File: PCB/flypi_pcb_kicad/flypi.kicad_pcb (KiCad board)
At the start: 2 copper layers, 76.1 x 85.1 mm, 44 parts, among them CON1 BARREL_JACK, J12 USB_A, P1 Pelt S1S2, P10 RGB BG-R, P3 Fan-+, P4 Therm -s+, P5 HP1 gnd vcc, P6 HP2 gnd vcc, P7 servo -s+, P8 Ring s-+, P9 I2C +-scsd, Q1 1A_NPN_ECB, Q2 1A-NPN-ECB, Q3 1A_NPN_ECB, Q4 1A_NPN_ECB, U1 LM2596, U2 LM2596, U4 L298N, U5 arduino_mini

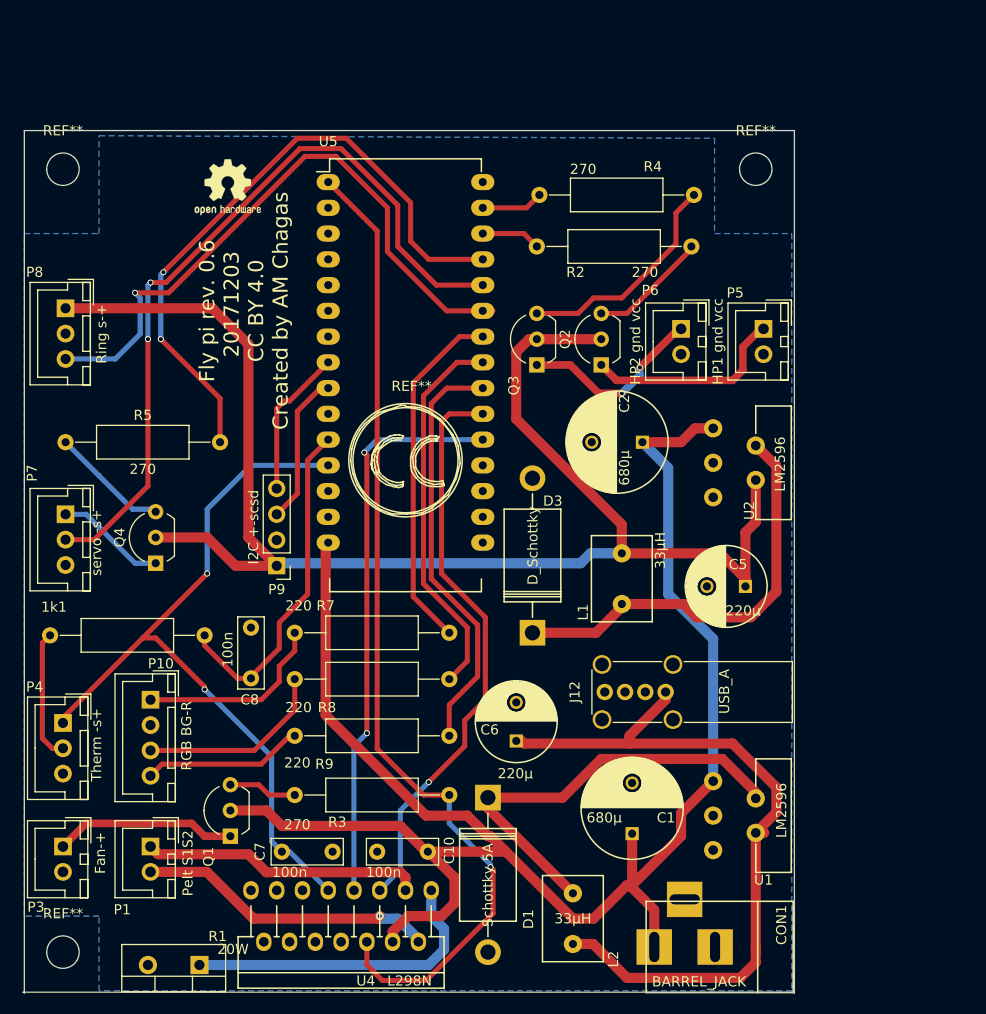
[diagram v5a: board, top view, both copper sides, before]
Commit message: updated pcb, so that screw holes are equidistant from board edges
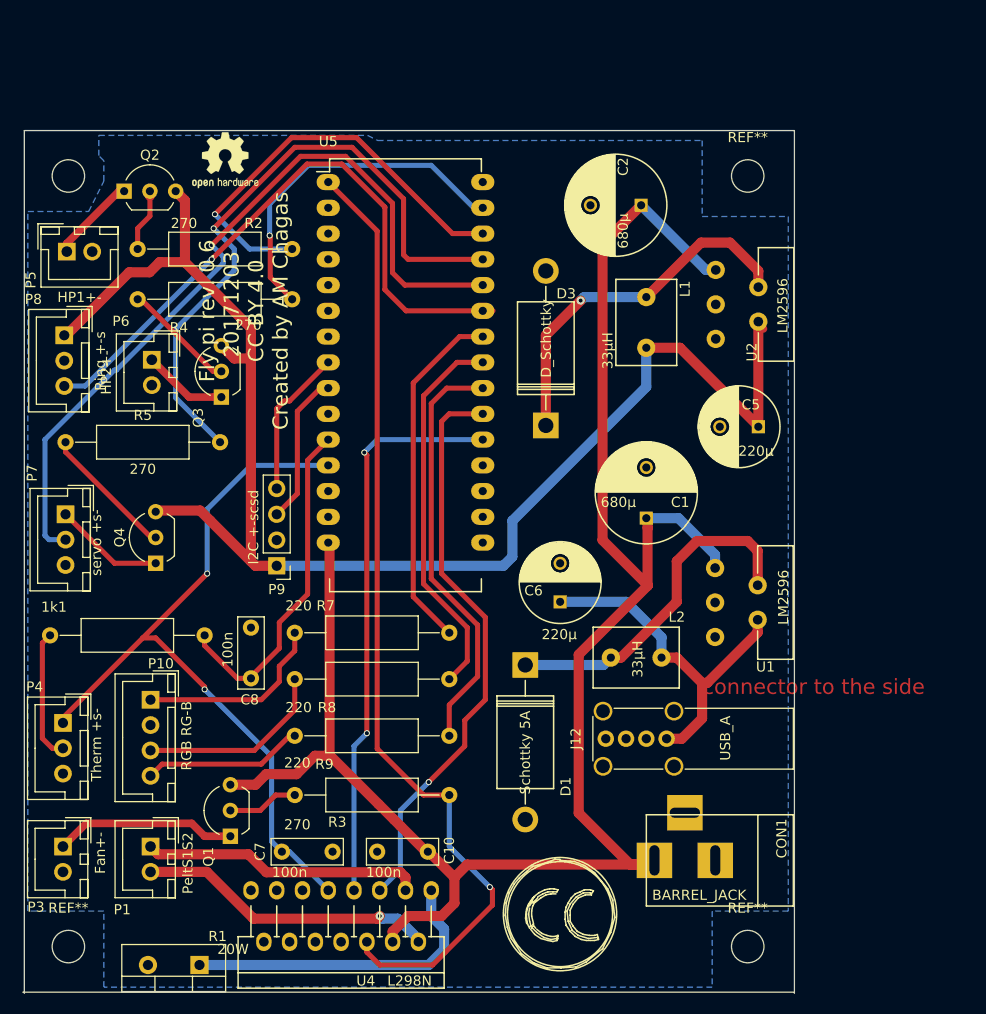
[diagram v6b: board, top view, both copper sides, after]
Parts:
- added REF**: MountingHole_3.2mm_M3_DIN965, Mounting_Holes:MountingHole_3.2mm_M3_DIN965, F.Cu at (176.5, 129.5)
-  : renamed from REF**; value MountingHole_3.2mm_M3_DIN965 -> (none)
- P1: value Pelt S1S2 -> PeltS1S2
- P10: value RGB BG-R -> RGB RG-B
- P3: value Fan-+ -> Fan+-
- P4: value Therm -s+ -> Therm +s-
- P5: value HP1 gnd vcc -> HP1+-
- P6: value HP2 gnd vcc -> HP2+-
- P7: value servo -s+ -> servo +s-
- P8: value Ring s-+ -> Ring +-s
- Q1, Q3, Q4: value 1A_NPN_ECB -> 1A_NPN_EBC
- Q2: value 1A-NPN-ECB -> 1A-NPN-EBC
- moved P5 69.1 mm to (109.3, 61.0), turned to 0 degrees
- moved R4 55.8 mm to (116.3, 65.7), turned to 0 degrees
- moved R2 54.6 mm to (116.3, 60.7), turned to 0 degrees
- moved P6 52.3 mm to (117.7, 71.6)
- moved Q2 50.1 mm to (115.0, 55.0), turned to 0 degrees
- moved ? 47.3 mm to (158.0, 126.3)
- moved Q3 31.3 mm to (124.6, 75.3)
- moved C1 31.1 mm to (166.5, 87.2)
- moved L2 26.5 mm to (165.5, 101.0), turned to 0 degrees
- moved L1 25.4 mm to (166.5, 67.9), turned to 270 degrees
- moved C2 23.4 mm to (166.0, 56.4)
- moved U1 21.0 mm to (177.5, 95.6)
- moved D3 20.5 mm to (156.6, 78.1)
- moved C5 15.8 mm to (177.5, 78.2)
- moved U2 15.6 mm to (177.5, 66.2)
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- renumbered REF** to ?
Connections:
- J12 pad 2: (no net) -> Net-(J12-Pad2)
- J12 pad 3: (no net) -> Net-(J12-Pad3)
- Q1 pad 2: Net-(C1-Pad1) -> Net-(Q1-Pad2)
- Q1 pad 3: Net-(Q1-Pad3) -> Net-(C1-Pad1)
- Q2 pad 2: Net-(C5-Pad1) -> Net-(Q2-Pad2)
- Q2 pad 3: Net-(Q2-Pad3) -> Net-(C5-Pad1)
- Q3 pad 2: Net-(C5-Pad1) -> Net-(Q3-Pad2)
- Q3 pad 3: Net-(Q3-Pad3) -> Net-(C5-Pad1)
- Q4 pad 2: Net-(C5-Pad1) -> Net-(Q4-Pad2)
- Q4 pad 3: Net-(Q4-Pad3) -> Net-(C5-Pad1)
- R2 pad 1: Net-(Q2-Pad3) -> Net-(Q2-Pad2)
- R3 pad 1: Net-(Q1-Pad3) -> Net-(Q1-Pad2)
- R4 pad 1: Net-(Q3-Pad3) -> Net-(Q3-Pad2)
- R5 pad 1: Net-(Q4-Pad3) -> Net-(Q4-Pad2)
- U4 pad 10: (no net) -> Net-(U4-Pad10)
- U4 pad 11: (no net) -> Net-(U4-Pad11)
- U4 pad 12: (no net) -> Net-(U4-Pad12)
- U4 pad 13: (no net) -> Net-(U4-Pad13)
- U4 pad 14: (no net) -> Net-(U4-Pad14)
- U4 pad 15: (no net) -> Net-(U4-Pad15)
- U5 pad 10: (no net) -> Net-(U5-Pad10)
- U5 pad 13: (no net) -> Net-(U5-Pad13)
- U5 pad 16: (no net) -> Net-(U5-Pad16)
- U5 pad 17: (no net) -> Net-(U5-Pad17)
- U5 pad 18: (no net) -> Net-(U5-Pad18)
- U5 pad 2: (no net) -> Net-(U5-Pad2)
- U5 pad 3: (no net) -> Net-(U5-Pad3)
- U5 pad 30: (no net) -> Net-(U5-Pad30)
- U5 pad 4: (no net) -> Net-(U5-Pad4)
- U5 pad 5: (no net) -> Net-(U5-Pad5)
- U5 pad 6: (no net) -> Net-(U5-Pad6)
- U5 pad 7: (no net) -> Net-(U5-Pad7)
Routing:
- net Net-(C6-Pad1): track 73.1 -> 35.1 mm
- net Net-(R2-Pad2): track 5.86 -> 42.5 mm, vias 0 -> 1
- net Net-(R4-Pad2): track 6.11 -> 34.7 mm, vias 0 -> 1
- net Net-(Q3-Pad3): track 22.1 -> 0.00 mm
- net Net-(Q4-Pad2): track 0.00 -> 13.3 mm
- net Net-(C1-Pad1): track 170.1 -> 182.8 mm
- net Net-(Q2-Pad3): track 11.8 -> 0.00 mm
- net Net-(Q4-Pad3): track 11.7 -> 0.00 mm
- net Net-(P5-Pad1): track 20.1 -> 8.59 mm
- net Net-(Q3-Pad2): track 0.00 -> 11.2 mm
- net Net-(P6-Pad1): track 18.5 -> 9.08 mm, vias 2 -> 0
- net Net-(D1-Pad1): track 42.9 -> 34.9 mm
- net Net-(Q2-Pad2): track 0.00 -> 7.13 mm
- net Net-(Q1-Pad2): track 0.00 -> 6.98 mm
- net Net-(Q1-Pad3): track 6.77 -> 0.00 mm
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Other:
- board text added: "connector side"
- board text added: "connector to the side"
- board text added: "top"

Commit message: update gebers
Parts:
- P10: value RGB RG-B -> RGB GB-R
- P3: value Fan+- -> Fan-+
- P4: value Therm +s- -> Therm -s+
- P6: value HP2+- -> HP2-+
- P7: value servo +s- -> servo -s+
- P8: value Ring +-s -> Ring s-+
- moved REF*** 0.66 mm to (125.0, 52.6)
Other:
- board text removed: "connector side"
- board text removed: "connector to the side"
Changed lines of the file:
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@@
-(kicad_pcb (version 4) (host pcbnew 4.0.7-e2-6376~58~ubuntu16.04.1)
+(kicad_pcb (version 4) (host pcbnew 4.0.2-stable)
   (general
     (links 87)
     (no_connects 0)
-    (area 68.900001 33.15499 212.635715 161.577001)
+    (area 68.750001 33.044987 212.785715 161.577001)
     (thickness 1.6)
-    (drawings 33)
+    (drawings 30)
     (tracks 301)
     (zones 0)
@@
       (drillshape 0)
       (scaleselection 1)
-      (outputdirectory /home/andre/Dropbox/code/repositories/prometheus_repos/Flypi/PCB/flypi_pcb_kicad/gerber1/))
+      (outputdirectory E:/Dropbox/code/repositories/prometheus_repos/Flypi/PCB/flypi_pcb_kicad/gerber1/))
   )
   (net 0 "")
@@
       (effects (font (size 1 1) (thickness 0.15)))
     )
-    (fp_text user %R (at 2.54 -3.56 270) (layer F.Fab)
+    (fp_text user %R (at -2.089 -2.187 270) (layer F.Fab)
       (effects (font (size 1 1) (thickness 0.15)))
     )
@@
       (effects (font (size 1 1) (thickness 0.15)))
     )
-    (fp_text value Fan+- (at 0.635 -3.683 270) (layer F.SilkS)
+    (fp_text value Fan-+ (at 2.766 -3.634 270) (layer F.SilkS)
       (effects (font (size 1 1) (thickness 0.15)))
     )
@@
       (effects (font (size 1 1) (thickness 0.15)))
     )
-    (fp_text value "Therm +s-" (at 2.159 -3.302 270) (layer F.SilkS)
+    (fp_text value "Therm -s+" (at 3.758 -3.634 270) (layer F.SilkS)
       (effects (font (size 1 1) (thickness 0.15)))
     )
@@
       (effects (font (size 1 1) (thickness 0.15)))
     )
-    (fp_text value "RGB RG-B" (at 3.556 -3.556 270) (layer F.SilkS)
+    (fp_text value "RGB GB-R" (at 3.556 -3.556 270) (layer F.SilkS)
       (effects (font (size 1 1) (thickness 0.15)))
     )
@@
       (effects (font (size 1 1) (thickness 0.15)))
     )
-    (fp_text value "Ring +-s" (at 2.54 -3.556 270) (layer F.SilkS)
+    (fp_text value "Ring s-+" (at 3.985 -3.507 270) (layer F.SilkS)
       (effects (font (size 1 1) (thickness 0.15)))
     )
@@
       (effects (font (size 1 1) (thickness 0.15)))
     )
-    (fp_text value "servo +s-" (at 2.794 -3.048 270) (layer F.SilkS)
+    (fp_text value "servo -s+" (at 2.794 -3.048 270) (layer F.SilkS)
       (effects (font (size 1 1) (thickness 0.15)))
     )
@@
       (effects (font (size 1 1) (thickness 0.15)))
     )
-    (fp_text value HP2+- (at 1.25 4.5 270) (layer F.SilkS)
+    (fp_text value HP2-+ (at 2.772 -3.471 270) (layer F.SilkS)
       (effects (font (size 1 1) (thickness 0.15)))
     )
@@
   )
   (module Symbols:OSHW-Logo2_7.3x6mm_SilkScreen (layer F.Cu)
-    (at 124.968 51.943)
+    (at 125 52.6)
     (descr "Open Source Hardware Symbol")
     (tags "Logo Symbol OSHW")
@@
     (arrow2b (pts (xy 197.5 50.5) (xy 198.086421 51.626504)))
   )
-  (gr_text "connector side" (at 190.627 129.667) (layer Cmts.User)
-    (effects (font (size 1.5 1.5) (thickness 0.3)))
-  )
   (dimension 7.747 (width 0.3) (layer Eco2.User)
     (gr_text "7,747 mm" (at 202.137 109.7915 90) (layer Eco2.User)
@@
     (effects (font (size 1.5 1.5) (thickness 0.3)))
   )
-  (gr_text "connector side" (at 190.246 103.505) (layer Cmts.User)
-    (effects (font (size 1.5 1.5) (thickness 0.3)))
-  )
-  (gr_text "connector to the side\n" (at 183.007 103.886) (layer F.Cu)
-    (effects (font (size 1.5 1.5) (thickness 0.3)))
-  )
   (dimension 75.819106 (width 0.3) (layer Eco2.User)
     (gr_text "75.819 mm" (at 143.083503 144.796684 0.09597274025) (layer Eco2.User)
@@
   (target plus (at 105.156 134.112) (size 5) (width 0.1) (layer Edge.Cuts))
   (target plus (at 181.05 134.05) (size 5) (width 0.1) (layer Edge.Cuts))
-  (gr_text "Fly pi rev. 0.6\n  20171203\nCC BY 4.0\nCreated by AM Chagas\n\n" (at 128.016 66.802 90) (layer F.SilkS)
+  (gr_text "Fly pi rev. 0.6\n  20171203\nCC BY 4.0\nCreated by AM Chagas\n\n" (at 143.6 72 90) (layer F.SilkS)
     (effects (font (size 1.5 1.5) (thickness 0.3)))
   )
